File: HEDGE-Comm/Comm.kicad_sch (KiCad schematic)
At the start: 3 parts, among them J1 ESQ-126-39-G-D, J2 ESQ-126-39-G-D, U1 STM32U595RJTx

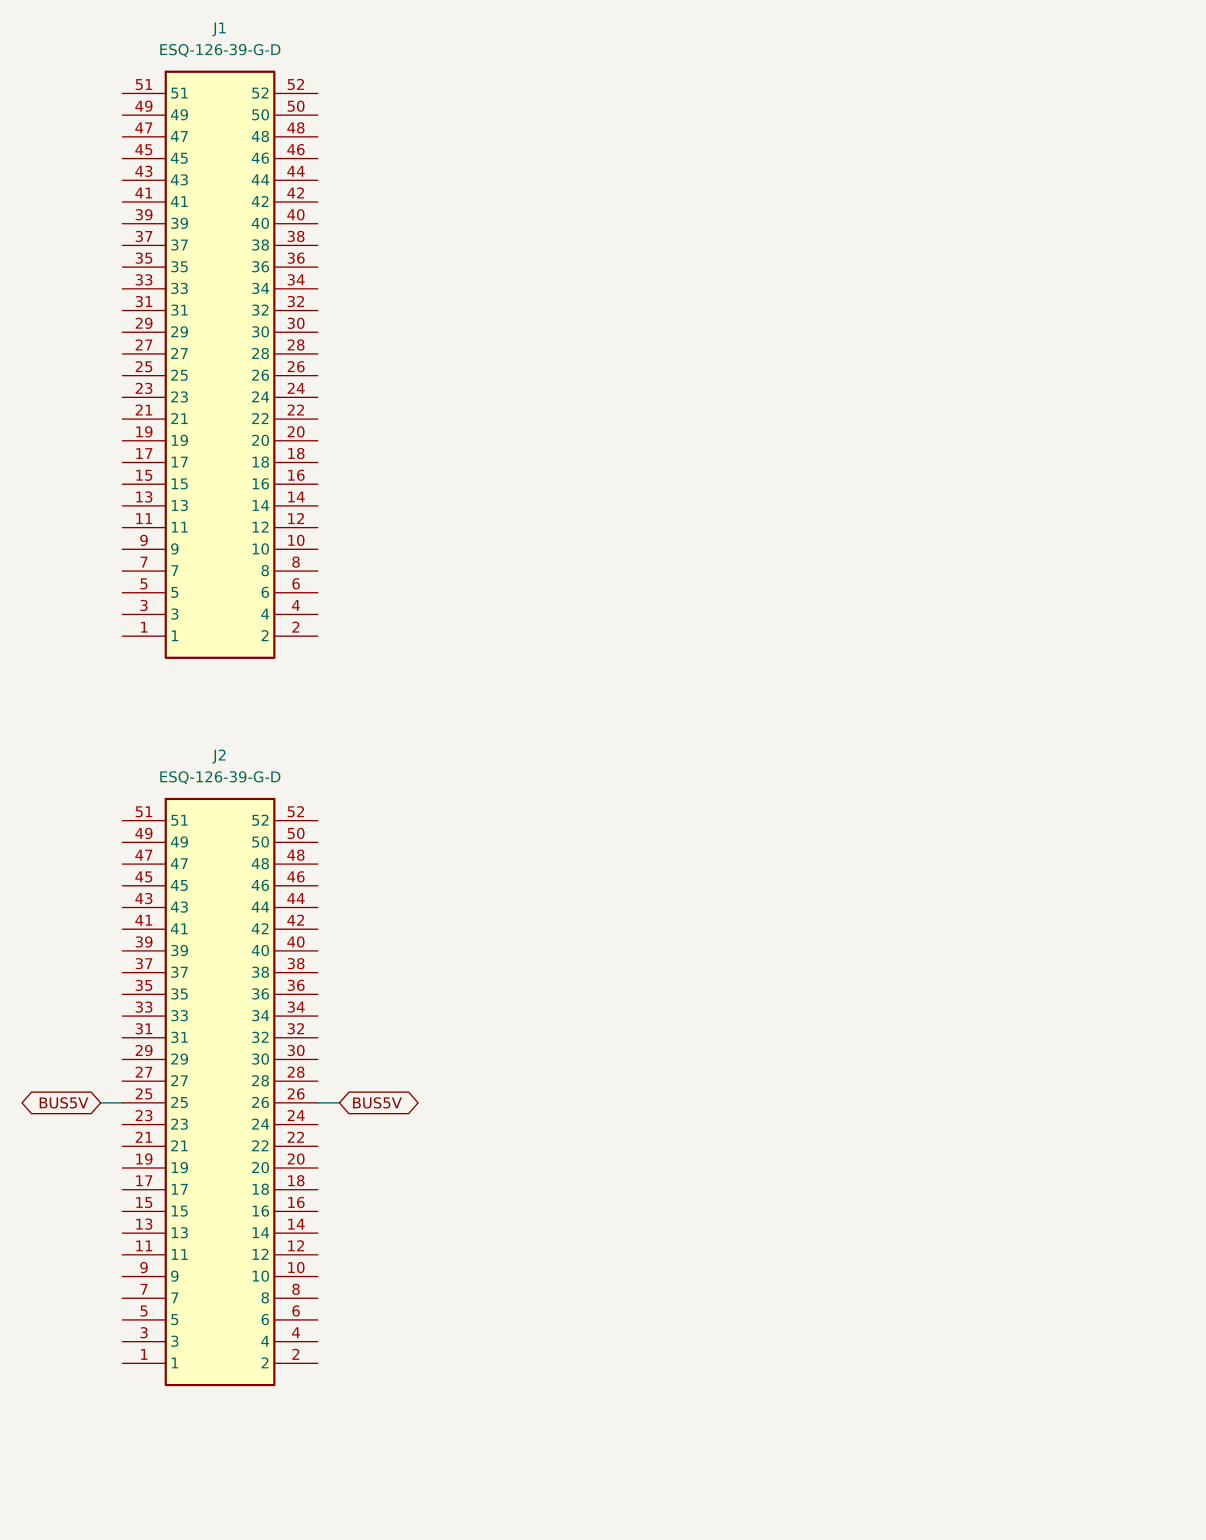
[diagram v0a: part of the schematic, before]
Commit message: Repair KiCAD files; modularize common circuits
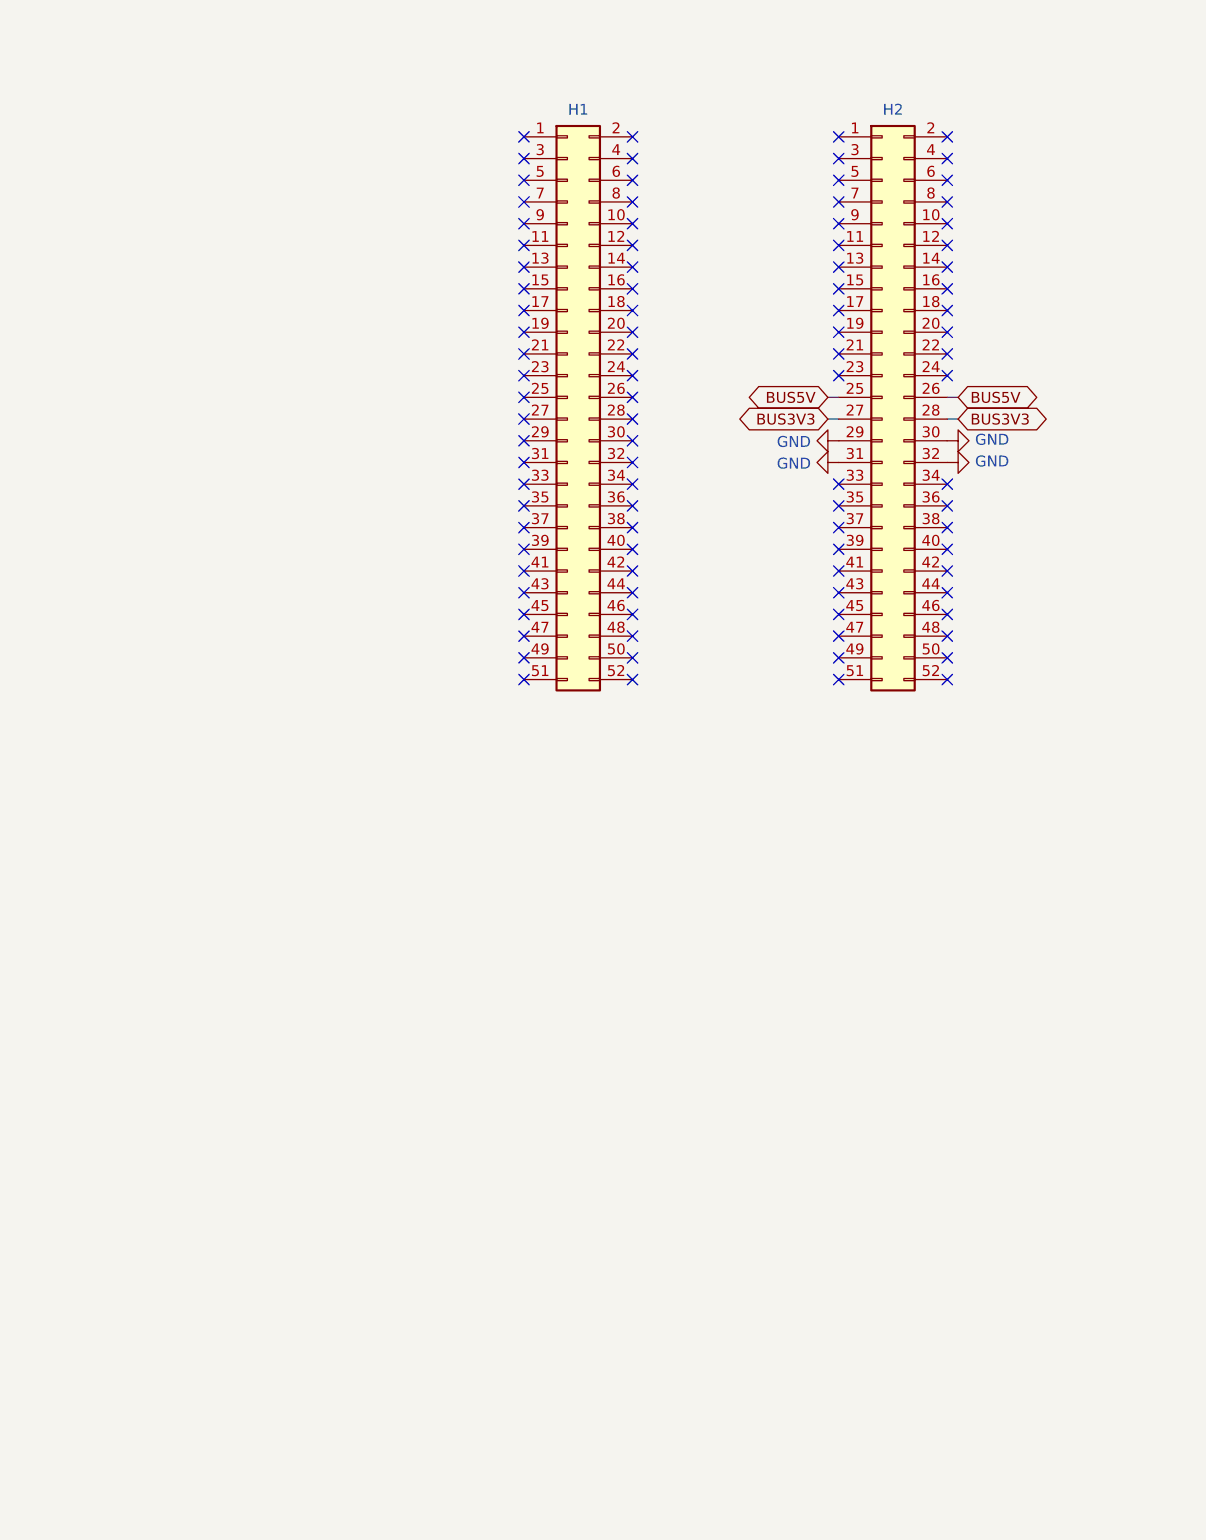
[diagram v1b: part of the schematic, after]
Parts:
- removed J1, J2: ESQ-126-39-G-D, ESQ-126-Y-X-D, symbol Bus:ESQ-126-39-G-D
- added H1, H2: Conn_02x26_Odd_Even, VST104_footprints:ESQ-126-39-x-D, symbol Connector_Generic:Conn_02x26_Odd_Even
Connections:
- net BUS5V: now also H2.25 (Pin_25), H2.26 (Pin_26)
- new net BUS3V3: H2.27 (Pin_27), H2.28 (Pin_28)
- new net GND: H2.29 (Pin_29), H2.30 (Pin_30), H2.31 (Pin_31), H2.32 (Pin_32)
- no-connect marks 0 -> 96

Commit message: Refactor Data PCB files; enter RS485; enter Iridium radio power
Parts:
- removed U1: STM32U595RJTx, Package_QFP:LQFP-64_10x10mm_P0.5mm, symbol MCU_ST_STM32U5:STM32U595RJTx
- added C23, C24: 220n, VST104_footprints:C_SMD_0402, symbol Device:C_Small
- added J1: U.FL-R-SMT-1_10_, Connector_Coaxial:U.FL_Hirose_U.FL-R-SMT-1_Vertical, symbol U.FL-R-SMT-1_10_:U.FL-R-SMT-1_10_
- added J2: SS4-10-3.50-X-D-K-TR, SS4-10-3.50-L-D-K-TR:SAMTEC_SS4-10-3.50-X-D-K-TR, symbol SS4-10-3.50-X-D-K-TR:SS4-10-3.50-X-D-K-TR
- added J3: Conn_Coaxial, Amphenol 132136:132136, symbol Connector:Conn_Coaxial
- added MH1, MH2, MH3, MH4: MountingHole_Pad, VST104_footprints:MountingHole_3.2mm_M3_Pad_Via, symbol Mechanical:MountingHole_Pad
- added Q1, Q3: DMG3415UFY4Q-7, DMG3415:DMG3415UFY47, symbol DMG3415UFY4Q-7:DMG3415UFY4Q-7
- added Q2, Q4, Q5: 2N2222AUB, 2N2222:SMD3_UB_MCH, symbol 2N2222AUB:2N2222AUB
- added R10, R12, R13, R15, R16, R18, R19: 10k, VST104_footprints:R_SMD_0402, symbol Device:R_Small
- added R11, R14, R17: 1k, VST104_footprints:R_SMD_0402, symbol Device:R_Small
- added U4: STM32U595RJTx, Package_QFP:LQFP-64_10x10mm_P0.5mm, symbol MCU_ST_STM32U5:STM32U595RJTx
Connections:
- net GND: now also C23.1, C24.1, J1.1, J2.03 (GND), J2.04 (GND), J2.08 (SIG_GND), J2.15 (SIG_GND), J2.18 (SIG_GND), J3.2 (Ext), Q2.2, Q4.2, Q5.2, R12.2, R15.2, R16.2, R18.2, R19.2
- net CANL: now reaches H1.1 (Pin_1)
- net CANH: now reaches H1.3 (Pin_3)
- net PAY1B: now reaches H1.34 (Pin_34)
- net PAY1A: now reaches H1.36 (Pin_36)
- new net: Q4.1, R14.1
- new net: Q3.1 (G), Q4.3, R13.2
- new net: U4.18 (VSS), U4.31 (VSS), U4.47 (VSS), U4.63 (VSS)
- new net: Q1.1 (G), Q2.3, R10.2
- new net: J2.01 (VCC), J2.02 (VCC), Q3.3 (D)
- new net: J2.05 (ON/OFF), Q5.3
- new net: J1.2, J3.1 (In)
- new net: Q2.1, R11.1
- new net: Q5.1, R17.1
- new net COMM_CTS: J2.11 (CTS)
- new net COMM_NET_AVAIL: J2.19 (NET_AVAIL), R18.1
- new net COMM_PWR1_EN: R11.2, R12.1
- new net COMM_PWR2_EN: R14.2, R15.1
- new net COMM_RI: J2.12 (RI)
- new net COMM_RTS: J2.13 (RTS)
- new net COMM_RX: J2.07 (RX_OUT)
- new net COMM_TX: J2.06 (TX_IN)
- new net COMM_XCVR_EN: R16.1, R17.2
- new net COMM_XCVR_IND: J2.20 (PWR_IND), R19.1
- new net INA260a/LOAD: C23.2, Q1.2 (S), R10.1
- new net INA260b/SOURCE: Q1.3 (D)
- new net INA260c/LOAD: C24.2, Q3.2 (S), R13.1
- no-connect marks 96 -> 99
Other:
- removed sheet INA740B
- added sheet INA260 (INA260.kicad_sch)
- added sheet INA260a (INA260.kicad_sch)
- added sheet INA260b (INA260.kicad_sch)
- added sheet INA260c (INA260.kicad_sch)
- added sheet LTC3225fb (LTC3225fb.kicad_sch)
- added sheet LTC3225fb1 (LTC3225fb.kicad_sch)
- added sheet RS485 (RS485.kicad_sch)
- company: (none) -> Spacecraft Design Lab
- title: (none) -> HEDGE Comm PCB
